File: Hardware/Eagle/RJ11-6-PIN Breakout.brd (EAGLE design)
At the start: 17.8 x 17.8 mm, 2 parts, among them J1 Amphenol MRJR-3460-0F

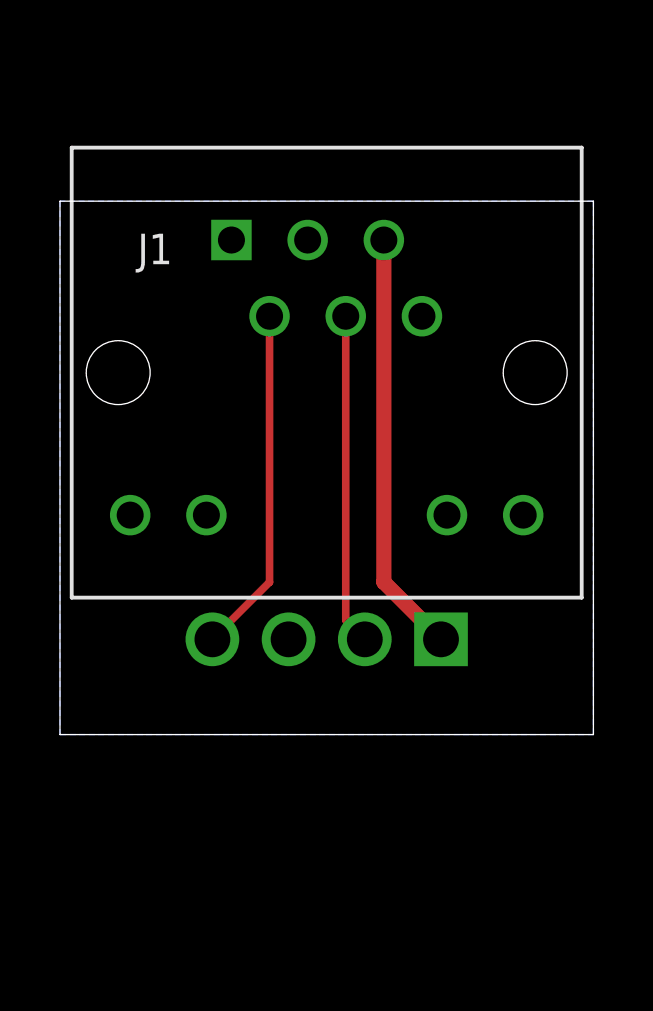
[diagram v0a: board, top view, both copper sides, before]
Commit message: Switched to a right angle connector on the RJ11 breakout
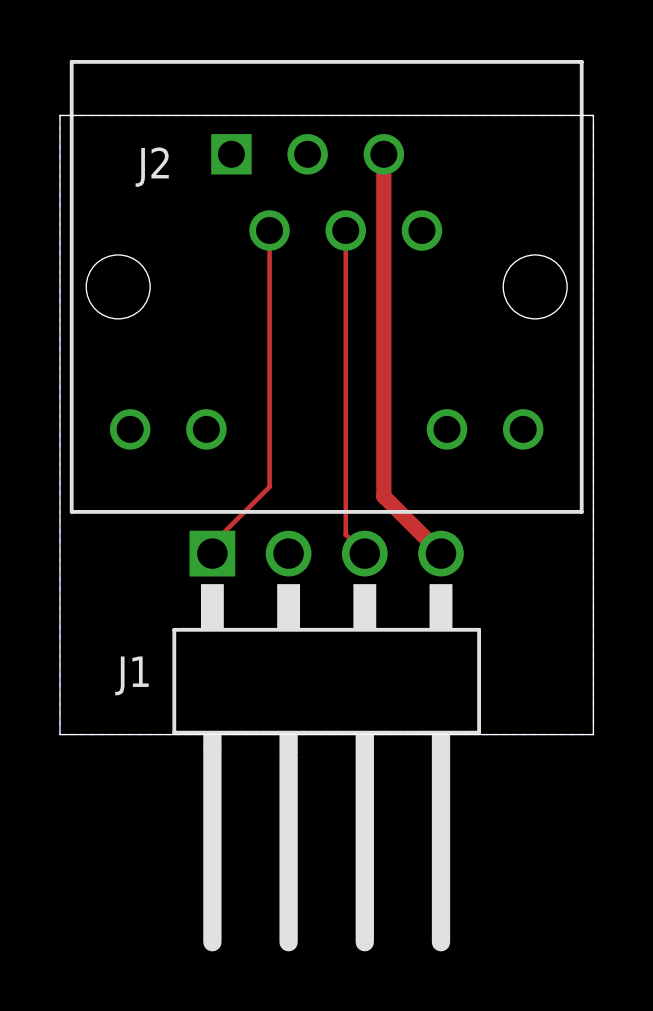
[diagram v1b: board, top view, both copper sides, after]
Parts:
- removed JP1: MOLEX 22112042, AUmlib:MOLEX-04-VERT
- added J2: Amphenol MRJR-3460-0F, AUmlib:RJ11-6-PIN
- J1: value Amphenol MRJR-3460-0F -> Molex 22122044; device AUmlib:RJ11-6-PIN -> AUmlib:1X04RA-MOLEX-22122044
- moved J1 9.92 mm to (10.2, 2.22)
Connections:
- net GND: now also J1.2, J2.3; no longer J1.3, JP1.3
- net RX: now also J1.3, J2.4; no longer J1.4, JP1.2
- net TX: now also J1.1, J2.2; no longer J1.2, JP1.4
- net VCC: now also J1.4, J2.5; no longer J1.5, JP1.1
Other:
- board size 17.8 x 17.8 mm -> 17.8 x 20.6 mm
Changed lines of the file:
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@@
 </layers>
 <board>
-<fusionsync huburn="a.cGVyc29uYWw6dWUyZDgyNjcx" projecturn="a.cGVyc29uYWw6dWUyZDgyNjcxIzIwMTgxMjIwMTY2NDc1MjMx" f3durn="urn:adsk.wipprod:dm.lineage:SILO-arIReG6jrEVXBfZUQ" pcbguid="" lastpulledtime="" lastsyncedchangeguid="" latestrevisionid="433838ef-a01e-4171-a3dc-25f855af5ae7" lastsyncedrevisionid="433838ef-a01e-4171-a3dc-25f855af5ae7" lastboardhashguid="feee290f-5940-1554-281c-ad54c160f4c3" lastpushedtime="2020-11-28T20:02:38Z" linktopcb3d="true"/>
+<fusionsync huburn="a.cGVyc29uYWw6dWUyZDgyNjcx" projecturn="a.cGVyc29uYWw6dWUyZDgyNjcxIzIwMTgxMjIwMTY2NDc1MjMx" f3durn="urn:adsk.wipprod:dm.lineage:SILO-arIReG6jrEVXBfZUQ" pcbguid="" lastpulledtime="" lastsyncedchangeguid="" latestrevisionid="29585204-a2a1-4612-8995-8d23753b975b" lastsyncedrevisionid="29585204-a2a1-4612-8995-8d23753b975b" lastboardhashguid="4d23337f-3755-2952-6923-9db0f8f3c9bc" lastpushedtime="2020-11-29T18:58:21Z" linktopcb3d="true"/>
 <plain>
 <wire x1="0" y1="0" x2="17.78" y2="0" width="0" layer="20"/>
-<wire x1="17.78" y1="0" x2="17.78" y2="17.78" width="0" layer="20"/>
-<wire x1="17.78" y1="17.78" x2="0" y2="17.78" width="0" layer="20"/>
-<wire x1="0" y1="17.78" x2="0" y2="0" width="0" layer="20"/>
-<text x="14.605" y="3.175" size="1.016" layer="22" rot="MR180">+5V</text>
-<text x="10.795" y="8.255" size="1.016" layer="22" rot="MR270">RX</text>
-<text x="8.255" y="8.89" size="1.016" layer="22" rot="MR270">GND</text>
-<text x="1.905" y="3.175" size="1.016" layer="22" rot="MR180">TX</text>
+<wire x1="17.78" y1="0" x2="17.78" y2="20.6375" width="0" layer="20"/>
+<wire x1="17.78" y1="20.6375" x2="0" y2="20.6375" width="0" layer="20"/>
+<wire x1="0" y1="20.6375" x2="0" y2="0" width="0" layer="20"/>
+<text x="14.605" y="6.0325" size="1.016" layer="22" rot="MR180">+5V</text>
+<text x="10.795" y="11.1125" size="1.016" layer="22" rot="MR270">RX</text>
+<text x="8.255" y="11.7475" size="1.016" layer="22" rot="MR270">GND</text>
+<text x="1.905" y="6.0325" size="1.016" layer="22" rot="MR180">TX</text>
 </plain>
 <attributes>
@@
 </autorouter>
 <elements>
-<element name="J1" library="AUmlib" library_urn="urn:adsk.eagle:library:9166017" package="RJ11-6-PIN" package3d_urn="urn:adsk.eagle:package:25057203/5" value="Amphenol MRJR-3460-0F" x="8.89" y="12.065" smashed="yes">
-<attribute name="NAME" x="2.585" y="15.68" size="1.016" layer="25"/>
+<element name="J2" library="AUmlib" library_urn="urn:adsk.eagle:library:9166017" package="RJ11-6-PIN" package3d_urn="urn:adsk.eagle:package:25057203/5" value="Amphenol MRJR-3460-0F" x="8.89" y="14.9225" smashed="yes">
+<attribute name="NAME" x="2.585" y="18.5375" size="1.016" layer="25"/>
 </element>
-<element name="JP1" library="AUmlib" library_urn="urn:adsk.eagle:library:9166017" package="MOLEX-04-VERT" package3d_urn="urn:adsk.eagle:package:16461091/3" value="MOLEX 22112042" x="8.89" y="3.175" smashed="yes" rot="MR0">
-<attribute name="NAME" x="10.16" y="1.27" size="1.016" layer="26" rot="MR0"/>
+<element name="J1" library="AUmlib" library_urn="urn:adsk.eagle:library:9166017" package="1X04RA-MOLEX-22122044" package3d_urn="urn:adsk.eagle:package:25075311/2" value="Molex 22122044" x="10.16" y="2.2225" smashed="yes">
+<attribute name="NAME" x="1.905" y="1.5875" size="1.016" layer="25" font="vector"/>
 </element>
 </elements>
 <signals>
 <signal name="TX">
-<contactref element="JP1" pad="4"/>
-<contactref element="J1" pad="2"/>
-<wire x1="6.985" y1="13.945" x2="6.985" y2="5.08" width="0.254" layer="1"/>
-<wire x1="6.985" y1="5.08" x2="5.08" y2="3.175" width="0.254" layer="1"/>
+<contactref element="J2" pad="2"/>
+<contactref element="J1" pad="1"/>
+<wire x1="6.985" y1="16.8025" x2="6.985" y2="8.255" width="0.1524" layer="1"/>
+<wire x1="6.985" y1="8.255" x2="5.08" y2="6.35" width="0.1524" layer="1"/>
+<wire x1="5.08" y1="6.35" x2="5.08" y2="6.0325" width="0.1524" layer="1"/>
 </signal>
 <signal name="GND">
-<contactref element="JP1" pad="3"/>
-<contactref element="J1" pad="3"/>
+<contactref element="J2" pad="3"/>
 <polygon width="0.1524" layer="16">
 <vertex x="0" y="0"/>
 <vertex x="17.78" y="0"/>
-<vertex x="17.78" y="17.78"/>
-<vertex x="0" y="17.78"/>
+<vertex x="17.78" y="20.6375"/>
+<vertex x="0" y="20.6375"/>
 </polygon>
+<contactref element="J1" pad="2"/>
 </signal>
 <signal name="RX">
-<contactref element="JP1" pad="2"/>
+<contactref element="J2" pad="4"/>
+<contactref element="J1" pad="3"/>
+<wire x1="9.525" y1="16.8025" x2="9.525" y2="6.6675" width="0.1524" layer="1"/>
+<wire x1="9.525" y1="6.6675" x2="10.16" y2="6.0325" width="0.1524" layer="1"/>
+</signal>
+<signal name="VCC">
+<contactref element="J2" pad="5"/>
 <contactref element="J1" pad="4"/>
-<wire x1="9.525" y1="13.945" x2="9.525" y2="3.81" width="0.254" layer="1"/>
-<wire x1="9.525" y1="3.81" x2="10.16" y2="3.175" width="0.254" layer="1"/>
-</signal>
-<signal name="VCC">
-<contactref element="JP1" pad="1"/>
-<contactref element="J1" pad="5"/>
-<wire x1="10.795" y1="16.485" x2="10.795" y2="5.08" width="0.508" layer="1"/>
-<wire x1="10.795" y1="5.08" x2="12.7" y2="3.175" width="0.508" layer="1"/>
+<wire x1="10.795" y1="7.9375" x2="12.7" y2="6.0325" width="0.508" layer="1"/>
+<wire x1="10.795" y1="19.3425" x2="10.795" y2="7.9375" width="0.508" layer="1"/>
 </signal>
 </signals>
